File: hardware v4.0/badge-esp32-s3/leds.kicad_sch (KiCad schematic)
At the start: 32 parts

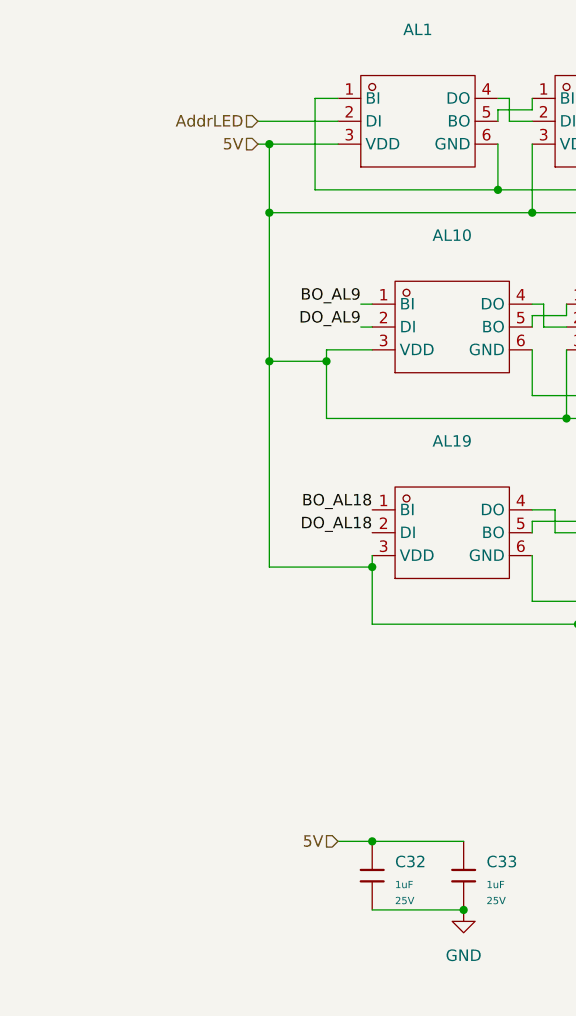
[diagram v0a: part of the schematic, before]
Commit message: started changes for 4.0.1
fixed footprint, joystick collision, Changed to Forced PWM mode for boost converter, Fixed some silkscreen errors
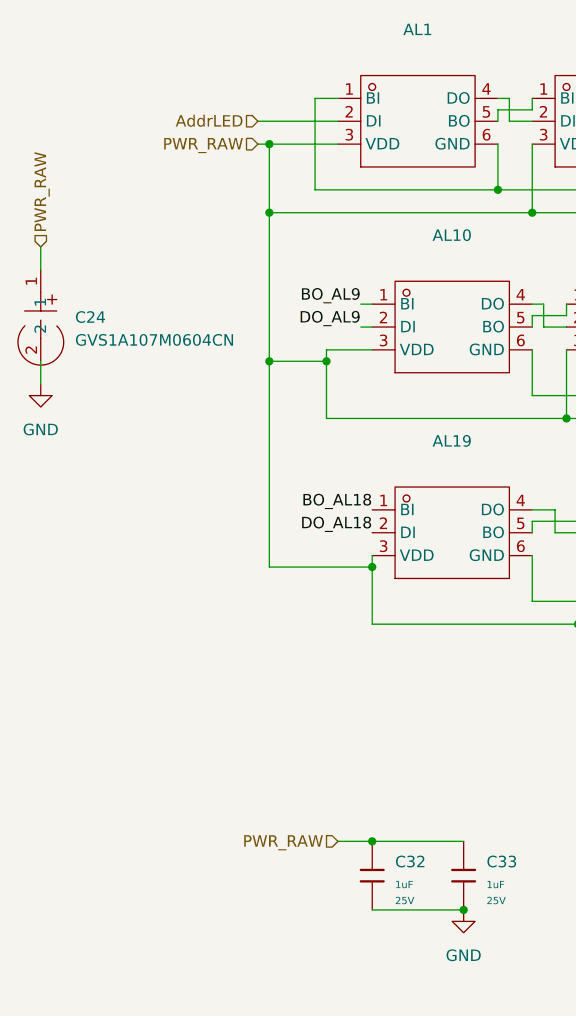
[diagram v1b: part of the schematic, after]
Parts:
- added C24: GVS1A107M0604CN, lcsc-lib:CAP-SMD_BD6.3-L6.6-W6.6-LS7.3-FD, symbol lcsc-lib:GVS1A107M0604CN
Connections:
- net GND: now also C24.2
- net 5V renamed PWR_RAW
- net PWR_RAW: now also C24.1
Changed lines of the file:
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@@
 	(wire
 		(pts
+			(xy 31.75 86.36) (xy 31.75 88.9)
+		)
+		(stroke
+			(width 0)
+			(type default)
+		)
+	)
+	(wire
+		(pts
 			(xy 226.06 85.09) (xy 226.06 92.71)
 		)
@@
 	(wire
 		(pts
+			(xy 31.75 73.66) (xy 31.75 76.2)
+		)
+		(stroke
+			(width 0)
+			(type default)
+		)
+	)
+	(wire
+		(pts
 			(xy 177.8 80.01) (xy 177.8 82.55)
 		)
@@
 		)
 	)
-	(hierarchical_label "5V"
+	(hierarchical_label "PWR_RAW"
 		(shape input)
-		(at 55.88 62.23 180)
+		(at 64.77 139.7 180)
 		(effects
 			(font
@@
 		)
 	)
-	(hierarchical_label "5V"
+	(hierarchical_label "PWR_RAW"
 		(shape input)
-		(at 64.77 139.7 180)
+		(at 55.88 62.23 180)
 		(effects
 			(font
@@
 		)
 	)
+	(hierarchical_label "PWR_RAW"
+		(shape input)
+		(at 31.75 73.66 90)
+		(effects
+			(font
+				(size 1.27 1.27)
+			)
+			(justify left)
+		)
+	)
 	(hierarchical_label "RGB_BLU"
 		(shape input)
@@
 	)
 	(symbol
+		(lib_id "lcsc-lib:GVS1A107M0604CN")
+		(at 31.75 81.28 270)
+		(unit 1)
+		(exclude_from_sim no)
+		(in_bom yes)
+		(on_board yes)
+		(dnp no)
+		(fields_autoplaced yes)
+		(property "Reference" "C24"
+			(at 35.56 81.4923 90)
+			(effects
+				(font
+					(size 1.27 1.27)
+				)
+				(justify left)
+			)
+		)
+		(property "Value" "GVS1A107M0604CN"
+			(at 35.56 84.0323 90)
+			(effects
+				(font
+					(size 1.27 1.27)
+				)
+				(justify left)
+			)
+		)
+		(property "Footprint" "lcsc-lib:CAP-SMD_BD6.3-L6.6-W6.6-LS7.3-FD"
+			(at 24.13 81.28 0)
+			(effects
+				(font
+					(size 1.27 1.27)
+				)
+				(hide yes)
+			)
+		)
+		(property "Datasheet" ""
+			(at 31.75 81.28 0)
+			(effects
+				(font
+					(size 1.27 1.27)
+				)
+				(hide yes)
+			)
+		)
+		(property "Description" ""
+			(at 31.75 81.28 0)
+			(effects
+				(font
+					(size 1.27 1.27)
+				)
+				(hide yes)
+			)
+		)
+		(property "LCSC Part" "C22383610"
+			(at 21.59 81.28 0)
+			(effects
+				(font
+					(size 1.27 1.27)
+				)
+				(hide yes)
+			)
+		)
+		(pin "1"
+		)
+		(pin "2"
+		)
+		(instances
+			(project ""
+				(path "/e2af9a6c-dbe9-4de2-9ba6-ea213a7300ec/cf4b41f4-37f8-453c-b748-b2fe0c3fb5a0"
+					(reference "C24")
+					(unit 1)
+				)
+			)
+		)
+	)
+	(symbol
 		(lib_id "lcsc-lib:WS2813B-2121")
 		(at 99.06 82.55 0)
@@
 					(unit 1)
 				)
+			)
+		)
+	)
+	(symbol
+		(lib_id "power:GND")
+		(at 31.75 88.9 0)
+		(unit 1)
+		(exclude_from_sim no)
+		(in_bom yes)
+		(on_board yes)
+		(dnp no)
+		(fields_autoplaced yes)
+		(property "Reference" "#PWR058"
+			(at 31.75 95.25 0)
+			(effects
+				(font
+					(size 1.27 1.27)
+				)
+				(hide yes)
+			)
+		)
+		(property "Value" "GND"
+			(at 31.75 93.98 0)
+			(effects
+				(font
+					(size 1.27 1.27)
+				)
+			)
+		)
+		(property "Footprint" ""
+			(at 31.75 88.9 0)
+			(effects
+				(font
+					(size 1.27 1.27)
+				)
+				(hide yes)
+			)
+		)
+		(property "Datasheet" ""
+			(at 31.75 88.9 0)
+			(effects
+				(font
+					(size 1.27 1.27)
+				)
+				(hide yes)
+			)
+		)
+		(property "Description" "Power symbol creates a global label with name \"GND\" , ground"
+			(at 31.75 88.9 0)
+			(effects
+				(font
+					(size 1.27 1.27)
+				)
+				(hide yes)
+			)
+		)
+		(pin "1"
+		)
+		(instances
+			(project "badge-esp32-s3"
+				(path "/e2af9a6c-dbe9-4de2-9ba6-ea213a7300ec/cf4b41f4-37f8-453c-b748-b2fe0c3fb5a0"
+					(reference "#PWR058")
+					(unit 1)
+				)

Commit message: added remainder of changes
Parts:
- removed R19: 5.1kΩ, PCM_JLCPCB:R_0402, symbol PCM_JLCPCB-Resistors:0402,5.1kΩ
- added R19: 470Ω, PCM_JLCPCB:R_0402, symbol PCM_JLCPCB-Resistors:0402,470Ω
- added U5: FRC1210F3R30TS, lcsc-lib:R1210, symbol lcsc-lib:FRC1210F3R30TS
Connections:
- net LED_SINGLE1: now also R19.1
- net PWR_RAW: now also U5.1; no longer AL1.3 (VDD), AL10.3 (VDD), AL11.3 (VDD), AL12.3 (VDD), AL13.3 (VDD), AL14.3 (VDD), AL15.3 (VDD), AL16.3 (VDD), AL17.3 (VDD), AL18.3 (VDD), AL19.3 (VDD), AL2.3 (VDD), AL20.3 (VDD), AL21.3 (VDD), AL22.3 (VDD), AL23.3 (VDD), AL24.3 (VDD), AL3.3 (VDD), AL4.3 (VDD), AL5.3 (VDD), AL6.3 (VDD), AL7.3 (VDD), AL8.3 (VDD), AL9.3 (VDD), C24.1, C32.1, C33.1
- net at D14.2: now also R19.2
- new net ADDR_LED_PWR: AL1.3 (VDD), AL10.3 (VDD), AL11.3 (VDD), AL12.3 (VDD), AL13.3 (VDD), AL14.3 (VDD), AL15.3 (VDD), AL16.3 (VDD), AL17.3 (VDD), AL18.3 (VDD), AL19.3 (VDD), AL2.3 (VDD), AL20.3 (VDD), AL21.3 (VDD), AL22.3 (VDD), AL23.3 (VDD), AL24.3 (VDD), AL3.3 (VDD), AL4.3 (VDD), AL5.3 (VDD), AL6.3 (VDD), AL7.3 (VDD), AL8.3 (VDD), AL9.3 (VDD), C24.1, C32.1, C33.1, U5.2
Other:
- note added: "3.3ohm resistor 500mW"
- moved on the sheet: C24
